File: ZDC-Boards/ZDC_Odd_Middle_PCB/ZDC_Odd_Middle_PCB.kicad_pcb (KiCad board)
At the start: 2 copper layers, 195.2 x 643 mm, 94 parts

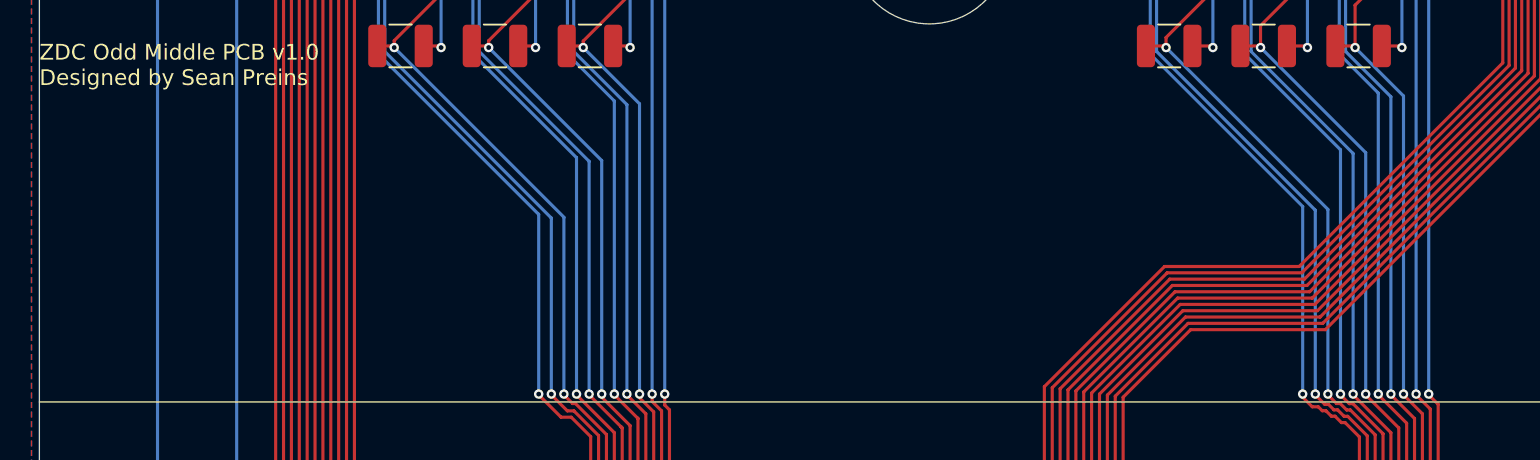
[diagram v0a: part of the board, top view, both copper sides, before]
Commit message: Updated small connector on ZDC PCBs
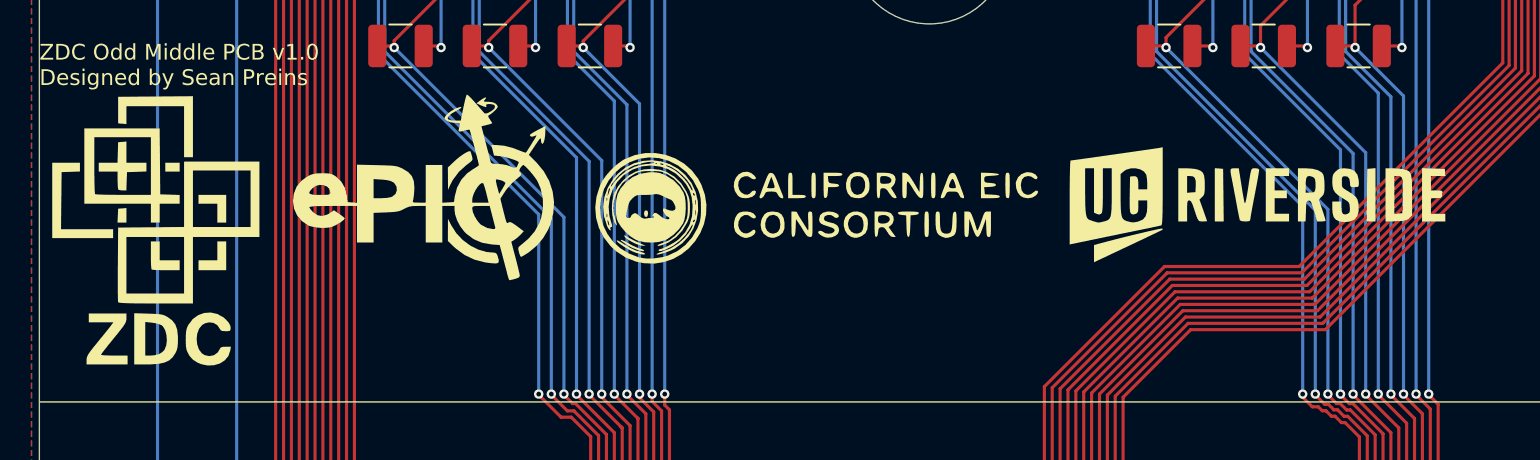
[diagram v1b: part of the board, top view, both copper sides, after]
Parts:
- added G***: LOGO, LOGO, F.Cu at (45.0, -599.0)
